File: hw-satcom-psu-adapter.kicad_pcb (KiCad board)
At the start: 2 copper layers, 89.2 x 45 mm, 37 parts, among them J1 Conn_01x04, J2 XT30, J3 XT30, J4 Conn_01x06_MountingPin, J5 s, U1 Brick-DCDC

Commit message: pmbus and normal
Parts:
- U1: footprint alex's:Quarter-Brick -> alex's:Quarter-Brick-PMBus
- moved R7 3.20 mm to (178.7, 82.1)
- moved R10 0.40 mm to (172.4, 95.5)
- moved R9 0.40 mm to (172.4, 98.5)
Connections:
- J5 pad 1: Net-(U1-Pad6) -> Net-(J5-Pad1)
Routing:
- net Net-(J5-Pad1): track 0.00 -> 25.8 mm, vias 0 -> 2
- net PMBus_ALT: track 43.0 -> 63.7 mm, vias 3 -> 2
- net Net-(R8-Pad2): track 0.00 -> 14.3 mm
- net GNDS: track 0.00 -> 12.4 mm
- net Net-(R7-Pad1): track 0.00 -> 11.0 mm
- net I2C_SCL: track 70.2 -> 63.0 mm, vias 1 -> 3
- net I2C_SDA: track 75.1 -> 68.1 mm
- net PMBus_CTL: track 36.1 -> 29.4 mm
- net +3V3: track 63.1 -> 64.6 mm
- net Net-(R10-Pad1): track 3.90 -> 3.29 mm
- net GND2: track 8.12 -> 8.51 mm, vias 2 -> 3

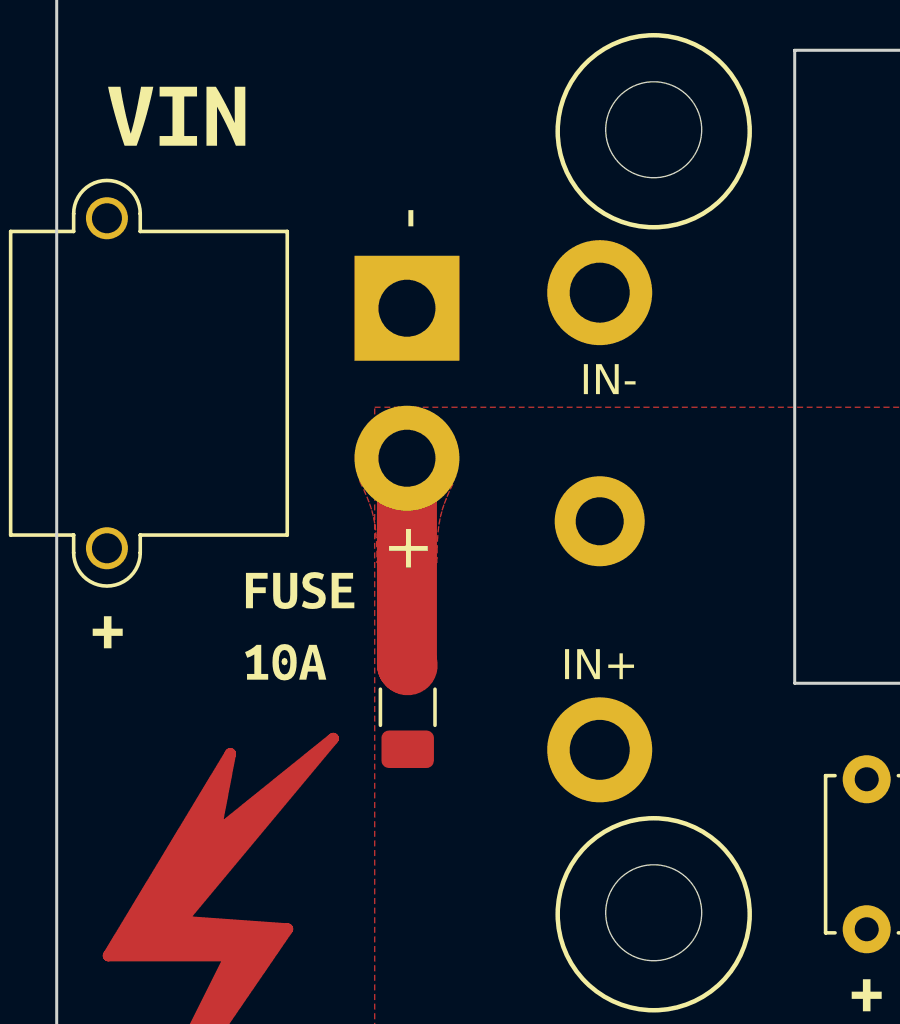
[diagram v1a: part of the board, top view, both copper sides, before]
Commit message: change fuse footprint
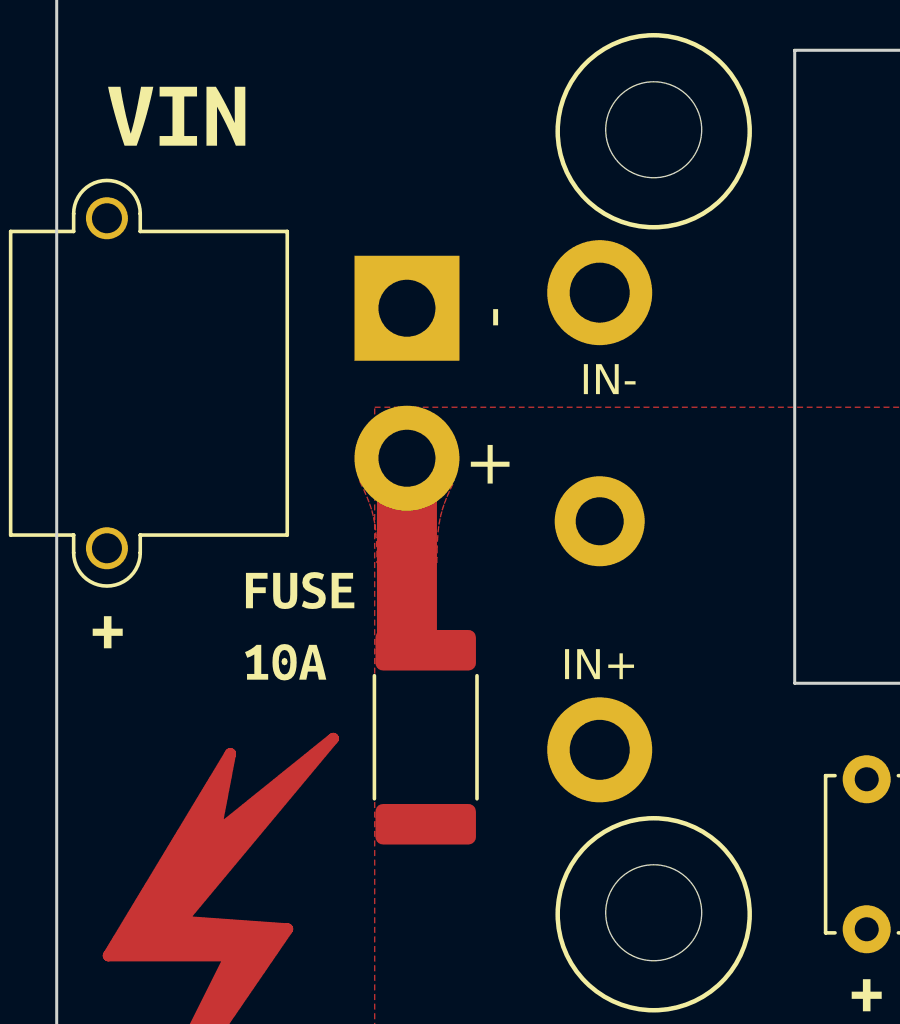
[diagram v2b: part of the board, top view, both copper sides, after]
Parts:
- F1: footprint Fuse:Fuse_1206_3216Metric -> Fuse:Fuse_2512_6332Metric
- moved F1 1.17 mm to (118.7, 104.1)
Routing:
- net Net-(F1-Pad1): track 6.91 -> 5.78 mm
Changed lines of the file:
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@@
       (effects (font (size 1 1) (thickness 0.15)))
     )
-    (fp_text user "-" (at 3 0 90) (layer "F.SilkS")
+    (fp_text user "-" (at -0.3 2.825 90) (layer "F.SilkS")
       (effects (font (size 1.5 1.5) (thickness 0.15)))
     )
-    (fp_text user "+" (at -8 0 90) (layer "F.SilkS")
+    (fp_text user "+" (at -5.2 2.725 90) (layer "F.SilkS")
       (effects (font (size 1.5 1.5) (thickness 0.15)))
     )
@@
     )
   )
-  (footprint "Fuse:Fuse_1206_3216Metric" (layer "F.Cu")
-    (at 118.1 103.1 -90)
-    (descr "Fuse SMD 1206 (3216 Metric), square (rectangular) end terminal, IPC_7351 nominal, (Body size source: http://www.tortai-tech.com/upload/download/2011102023233369053.pdf), generated with kicad-footprint-generator")
+  (footprint "Fuse:Fuse_2512_6332Metric" (layer "F.Cu")
+    (at 118.7 104.1 -90)
+    (descr "Fuse SMD 2512 (6332 Metric), square (rectangular) end terminal, IPC_7351 nominal, (Body size source: http://www.tortai-tech.com/upload/download/2011102023233369053.pdf), generated with kicad-footprint-generator")
     (tags "fuse")
     (property "Sheetfile" "hw-satcom-psu-adapter.kicad_sch")
     (property "Sheetname" "")
     (attr smd)
-    (fp_text reference "F1" (at 0 -1.82 90) (layer "F.SilkS") hide
-      (effects (font (size 1 1) (thickness 0.15)))
-    )
-    (fp_text value "10A" (at 0 1.82 90) (layer "F.Fab")
-      (effects (font (size 1 1) (thickness 0.15)))
-    )
-    (fp_text user "${REFERENCE}" (at 0 0 90) (layer "F.Fab") hide
-      (effects (font (size 0.8 0.8) (thickness 0.12)))
-    )
-    (fp_line (start -0.602064 -0.91) (end 0.602064 -0.91) (layer "F.SilkS") (width 0.12))
-    (fp_line (start -0.602064 0.91) (end 0.602064 0.91) (layer "F.SilkS") (width 0.12))
-    (fp_line (start -2.28 -1.12) (end 2.28 -1.12) (layer "F.CrtYd") (width 0.05))
-    (fp_line (start 2.28 -1.12) (end 2.28 1.12) (layer "F.CrtYd") (width 0.05))
-    (fp_line (start -2.28 1.12) (end -2.28 -1.12) (layer "F.CrtYd") (width 0.05))
-    (fp_line (start 2.28 1.12) (end -2.28 1.12) (layer "F.CrtYd") (width 0.05))
-    (fp_line (start 1.6 -0.8) (end 1.6 0.8) (layer "F.Fab") (width 0.1))
-    (fp_line (start -1.6 -0.8) (end 1.6 -0.8) (layer "F.Fab") (width 0.1))
-    (fp_line (start 1.6 0.8) (end -1.6 0.8) (layer "F.Fab") (width 0.1))
-    (fp_line (start -1.6 0.8) (end -1.6 -0.8) (layer "F.Fab") (width 0.1))
-    (pad "1" smd roundrect (at -1.4 0 270) (size 1.25 1.75) (layers "F.Cu" "F.Paste" "F.Mask") (roundrect_rratio 0.2)
+    (fp_text reference "F1" (at 0 -2.62 -90) (layer "F.SilkS") hide
+      (effects (font (size 1 1) (thickness 0.15)))
+    )
+    (fp_text value "10A" (at 0 2.62 -90) (layer "F.Fab")
+      (effects (font (size 1 1) (thickness 0.15)))
+    )
+    (fp_text user "${REFERENCE}" (at 0 0 -90) (layer "F.Fab")
+      (effects (font (size 1 1) (thickness 0.15)))
+    )
+    (fp_line (start -2.052064 1.71) (end 2.052064 1.71) (layer "F.SilkS") (width 0.12))
+    (fp_line (start -2.052064 -1.71) (end 2.052064 -1.71) (layer "F.SilkS") (width 0.12))
+    (fp_line (start -3.82 -1.92) (end 3.82 -1.92) (layer "F.CrtYd") (width 0.05))
+    (fp_line (start 3.82 -1.92) (end 3.82 1.92) (layer "F.CrtYd") (width 0.05))
+    (fp_line (start -3.82 1.92) (end -3.82 -1.92) (layer "F.CrtYd") (width 0.05))
+    (fp_line (start 3.82 1.92) (end -3.82 1.92) (layer "F.CrtYd") (width 0.05))
+    (fp_line (start -3.15 1.6) (end -3.15 -1.6) (layer "F.Fab") (width 0.1))
+    (fp_line (start 3.15 1.6) (end -3.15 1.6) (layer "F.Fab") (width 0.1))
+    (fp_line (start 3.15 -1.6) (end 3.15 1.6) (layer "F.Fab") (width 0.1))
+    (fp_line (start -3.15 -1.6) (end 3.15 -1.6) (layer "F.Fab") (width 0.1))
+    (pad "1" smd roundrect (at -2.9 0 270) (size 1.35 3.35) (layers "F.Cu" "F.Paste" "F.Mask") (roundrect_rratio 0.185185)
       (net 9 "Net-(F1-Pad1)") (pintype "passive"))
-    (pad "2" smd roundrect (at 1.4 0 270) (size 1.25 1.75) (layers "F.Cu" "F.Paste" "F.Mask") (roundrect_rratio 0.2)
+    (pad "2" smd roundrect (at 2.9 0 270) (size 1.35 3.35) (layers "F.Cu" "F.Paste" "F.Mask") (roundrect_rratio 0.185185)
       (net 1 "/VIN") (pintype "passive"))
-    (model "${KICAD6_3DMODEL_DIR}/Fuse.3dshapes/Fuse_1206_3216Metric.wrl"
+    (model "${KICAD6_3DMODEL_DIR}/Fuse.3dshapes/Fuse_2512_6332Metric.wrl"
       (offset (xyz 0 0 0))
       (scale (xyz 1 1 1))
@@
   (gr_rect (start 177.8 102.5) (end 180.7 87.5) (layer "B.Mask") (width 0.15) (fill solid))
   (gr_circle (center 185.4 82) (end 185.8 82) (layer "B.Mask") (width 0.15) (fill solid))
-  (gr_rect (start 117.1 97.2) (end 119 100.4) (layer "F.Mask") (width 0.15) (fill solid))
+  (gr_rect (start 117.1 97.2) (end 119 99.7) (layer "F.Mask") (width 0.15) (fill solid))
   (gr_rect (start 119 100.4) (end 119 100.4) (layer "F.Mask") (width 0.15) (fill none))
   (gr_rect (start 106.9 103.5) (end 116.1 119.3) (layer "F.Mask") (width 0.15) (fill solid))
   (gr_rect (start 178.1 95.1) (end 180.7 106.5) (layer "F.Mask") (width 0.15) (fill solid))
-  (gr_rect (start 119.8 107.3) (end 121.8 102.9) (layer "F.Mask") (width 0.15) (fill solid))
+  (gr_rect (start 122 110.6) (end 117.6 108.6) (layer "F.Mask") (width 0.15) (fill solid))
   (gr_line (start 131 102.3) (end 136.7 102.3) (layer "Edge.Cuts") (width 0.1))
   (gr_line (start 169.4 113.9) (end 169.4 102.4) (layer "Edge.Cuts") (width 0.1))
@@
   (segment (start 185.6525 88.965) (end 184.07 87.3825) (width 0.25) (layer "F.Cu") (net 8))
   (segment (start 185.7 88.965) (end 185.6525 88.965) (width 0.25) (layer "F.Cu") (net 8))
-  (segment (start 118.075 101.675) (end 118.1 101.7) (width 2) (layer "F.Cu") (net 9))
-  (segment (start 118.075 94.8) (end 118.075 101.675) (width 2) (layer "F.Cu") (net 9))
+  (segment (start 118.075 94.8) (end 118.075 100.575) (width 2) (layer "F.Cu") (net 9))
   (segment (start 189.15 110.775) (end 188.025 110.775) (width 0.2) (layer "F.Cu") (net 10))
   (segment (start 155.58 120.3) (end 154.88 119.6) (width 0.25) (layer "F.Cu") (net 10))

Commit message: ATX
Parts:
- removed C2, C3: 470uF/50V, Capacitor_THT:C_Disc_D5.0mm_W2.5mm_P5.00mm
- removed C4: 1uF/50V, Capacitor_SMD:C_0805_2012Metric
- removed F1: 10A, Fuse:Fuse_2512_6332Metric
- removed H1: MountingHole, MountingHole:MountingHole_2.5mm
- removed R10, R9: NC, Resistor_SMD:R_0603_1608Metric
- removed REF**: Symbol_HighVoltage_Type1_CopperTop_Big, Symbol:Symbol_HighVoltage_Type1_CopperTop_Big
- removed kibuzzard-6276051F: G***, kibuzzard-6276051F
- removed kibuzzard-6276052C: G***, kibuzzard-6276052C
- removed kibuzzard-62760583 (x5): G***, kibuzzard-62760583
- removed kibuzzard-62760647: G***, kibuzzard-62760647
- removed kibuzzard-62760724: G***, kibuzzard-62760724
- removed kibuzzard-62760775: G***, kibuzzard-62760775
- added C10: 470uF/25V, Capacitor_THT:CP_Radial_D6.3mm_P2.50mm, B.Cu at (183.4, 69.8)
- added C12: 470uF/25V, Capacitor_THT:CP_Radial_D6.3mm_P2.50mm, B.Cu at (208.2, 95.4)
- added C13: 470uF/25V, Capacitor_THT:CP_Radial_D6.3mm_P2.50mm, B.Cu at (218.5, 128.1)
- added C14: 100nF/100V, lc:0805_C, F.Cu at (113.7, 120.4)
- added C15: 470uF/25V, Capacitor_THT:CP_Radial_D6.3mm_P2.50mm, B.Cu at (217.5, 69.6)
- added C16: 470uF/25V, Capacitor_THT:CP_Radial_D6.3mm_P2.50mm, B.Cu at (217.4, 79.0)
- added C17: 470uF/25V, Capacitor_THT:CP_Radial_D6.3mm_P2.50mm, B.Cu at (216.6, 95.4)
- added C5: 47nF, lc:0402_C, F.Cu at (104.5, 111.7)
- added C6: 10nF, lc:0402_C, F.Cu at (103.5, 111.7)
- added C7: 470uF/25V, Capacitor_THT:CP_Radial_D6.3mm_P2.50mm, B.Cu at (200.7, 69.8)
- added C8: 470uF/25V, Capacitor_THT:CP_Radial_D6.3mm_P2.50mm, B.Cu at (192.1, 69.8)
- added C9: 470uF/25V, Capacitor_THT:CP_Radial_D6.3mm_P2.50mm, B.Cu at (174.8, 69.8)
- added D10: Green, lc:0805_LED_S1_NUM, F.Cu at (189.1, 128.7)
- added D11: Blue, lc:0805_LED_S1_NUM, F.Cu at (193.1, 128.7)
- added D12: Blue, lc:0805_LED_S1_NUM, F.Cu at (188.9, 119.1)
- added D4: Yellow, lc:0805_LED_S1_NUM, F.Cu at (181.1, 119.1)
- added D5: Yellow, lc:0805_LED_S1_NUM, F.Cu at (185.0, 119.1)
- added D6: 1N5819WS, lc:SOD-323, F.Cu at (162.4, 120.1)
- added D7: 1N5819WS, lc:SOD-323, F.Cu at (160.8, 120.1)
- added D8: Green, lc:0805_LED_S1_NUM, F.Cu at (181.2, 128.7)
- added D9: Green, lc:0805_LED_S1_NUM, F.Cu at (185.2, 128.7)
- added FL1: ACM1513F-551T100, t123yh:ACM1513, F.Cu at (122.7, 116.0)
- added G***: LOGO, LOGO, F.Cu at (160.6, 93.1)
- added H2: SMTSO-M3, MountingHole:MountingHole_4.3mm_M4_Pad, B.Cu at (106.5, 101.8)
- added H3: SMTSO-M3, MountingHole:MountingHole_4.3mm_M4_Pad, B.Cu at (106.4, 61.8)
- added H4: SMTSO-632, MountingHole:MountingHole_5.5mm_Pad, B.Cu at (229.3, 56.5)
- added H5: SMTSO-632, MountingHole:MountingHole_5.5mm_Pad, B.Cu at (91.8, 120.2)
- added H6: SMTSO-632, MountingHole:MountingHole_5.5mm_Pad, B.Cu at (91.5, 56.2)
- added H7: SMTSO-632, MountingHole:MountingHole_5.5mm_Pad, B.Cu at (205.3, 129.7)
- added H8: SMTSO-M3, MountingHole:MountingHole_4.3mm_M4_Pad, F.Cu at (171.6, 129.9)
- added H9: SMTSO-M3, MountingHole:MountingHole_4.3mm_M4_Pad, F.Cu at (122.8, 130.0)
- added J_CPU1: Conn_02x04_Top_Bottom, t123yh:ATX-8P, B.Cu at (201.4, 59.5)
- added J_CPU2: Conn_02x04_Top_Bottom, t123yh:ATX-8P, B.Cu at (180.5, 59.5)
- added Q1: NCE0140K2, Package_TO_SOT_SMD:TO-252-2, F.Cu at (90.1, 106.0)
- added Q2: NCE0140K2, Package_TO_SOT_SMD:TO-252-2, F.Cu at (100.5, 129.5)
- added Q3: NCE0140K2, Package_TO_SOT_SMD:TO-252-2, F.Cu at (97.5, 106.0)
- added Q4: 2N7002, Package_TO_SOT_SMD:SOT-23, F.Cu at (144.7, 120.6)
- added Q5: 2N7002, Package_TO_SOT_SMD:SOT-23, F.Cu at (156.8, 117.1)
- added Q6: 2N7002, Package_TO_SOT_SMD:SOT-23, F.Cu at (197.4, 133.2)
- added R11: 8.2k, lc:0402_R, F.Cu at (105.7, 111.7)
- added R12: 220k, lc:0603_R, F.Cu at (110.7, 107.2)
- added R13: 51k, lc:0402_R, F.Cu at (110.1, 122.2)
- added R14: 120k, lc:0603_R, F.Cu at (134.8, 116.9)
- added R15: 3m, lc:2512_R, F.Cu at (100.6, 117.4)
- added R16: 10k, lc:0402_R, F.Cu at (111.4, 122.2)
- added R17: 220k, lc:0603_R, F.Cu at (121.2, 96.9)
- added R18: 51k, lc:0603_R, F.Cu at (131.1, 118.3)
- added R19: 22k, lc:0402_R, F.Cu at (141.9, 120.7)
- added R20: 5.1k, lc:0402_R, F.Cu at (147.9, 122.1)
- added R21: 5.1k, lc:0402_R, F.Cu at (152.6, 118.5)
- added R22: 8.2k, lc:0402_R, F.Cu at (185.5, 114.7)
- added R23: 22k, lc:0402_R, F.Cu at (163.4, 123.0)
- added R24: 10k, lc:0603_R, F.Cu at (161.7, 117.1)
- added R25: 390, lc:0603_R, F.Cu at (214.4, 64.8)
- added R26: 100, lc:0402_R, F.Cu at (206.1, 79.1)
- added R27: 100, lc:0402_R, F.Cu at (217.0, 90.7)
- added U10: ZXDN10, t123yh:ZXDN10, B.Cu at (206.8, 90.6)
- added U2: TPS2350, Package_SO:TSSOP-14_4.4x5mm_P0.65mm, F.Cu at (106.4, 117.6)
- added U3: EL3H7(B)(TA)-G, Package_SO:SOP-4_4.4x2.6mm_P1.27mm, F.Cu at (108.3, 125.5)
- added U4: EL3H7(B)(TA)-G, Package_SO:SOP-4_4.4x2.6mm_P1.27mm, F.Cu at (136.4, 123.3)
- added U5: AV10-48S05, t123yh:AV10-48Sxx, B.Cu at (141.9, 64.3)
- added U6: EL3H7(B)(TA)-G, Package_SO:SOP-4_4.4x2.6mm_P1.27mm, F.Cu at (136.4, 119.6)
- added U7: TPS3510, Package_SO:SOIC-8_3.9x4.9mm_P1.27mm, F.Cu at (155.0, 121.9)
- added U8: ZXDN10, t123yh:ZXDN10, B.Cu at (214.5, 52.9)
- added U9: ZXDN10, t123yh:ZXDN10, B.Cu at (206.1, 68.9)
- D1: value Yellow -> Green; footprint LED_SMD:LED_0603_1608Metric -> lc:0805_LED_S1_NUM
- D2: value Yellow -> Red; footprint LED_SMD:LED_0603_1608Metric -> lc:0805_LED_S1_NUM
- D3: value Yellow -> 1N4148WS; footprint LED_SMD:LED_0603_1608Metric -> lc:SOD-323
- J1: value Conn_01x04 -> Conn_01x02_Male; footprint Connector_PinSocket_2.54mm:PinSocket_1x04_P2.54mm_Vertical -> Connector_AMASS:AMASS_XT60-M_1x02_P7.20mm_Vertical; moved to F.Cu
- J2: value XT30 -> ATX-24; footprint Connector_AMASS:AMASS_XT30PW-M_1x02_P2.50mm_Horizontal -> t123yh:ATX-24P; moved to B.Cu
- J3: value XT30 -> Conn_02x02_Top_Bottom; footprint Connector_AMASS:AMASS_XT30PW-M_1x02_P2.50mm_Horizontal -> t123yh:ATX-4P; moved to B.Cu
- J4: value Conn_01x06_MountingPin -> Conn_02x02_Top_Bottom; footprint Connector_Molex:Molex_CLIK-Mate_502382-0670_1x06-1MP_P1.25mm_Vertical -> t123yh:ATX-4P; moved to B.Cu
- J5: value s -> Conn_01x02_Male; footprint Connector_Molex:Molex_CLIK-Mate_502382-0370_1x03-1MP_P1.25mm_Vertical -> Connector_AMASS:AMASS_XT60-M_1x02_P7.20mm_Vertical
- R1: value 4.7k -> 200k; footprint Resistor_SMD:R_0603_1608Metric -> lc:0402_R
- R2: value 4.7k -> 22k; footprint Resistor_SMD:R_0603_1608Metric -> lc:0402_R
- R3: value 4.7k -> 56k; footprint Resistor_SMD:R_0603_1608Metric -> lc:0402_R
- R4: value 3.9k -> 56k; footprint Resistor_SMD:R_0603_1608Metric -> lc:0402_R
- R5: value 100k -> 390k; footprint Resistor_SMD:R_0603_1608Metric -> lc:0603_R
- R6: value 47k -> 5.6k; footprint Resistor_SMD:R_0603_1608Metric -> lc:0402_R
- R7, R8: value NC -> 3.3k; footprint Resistor_SMD:R_0603_1608Metric -> lc:0402_R
- kibuzzard-62760563: moved to B.Cu
- moved J2 109.0 mm to (227.0, 93.8)
- moved J5 89.0 mm to (102.7, 74.8), turned to 0 degrees
- moved R6 82.1 mm to (107.2, 112.1), turned to 180 degrees
- moved D3 78.7 mm to (110.3, 115.5), turned to 90 degrees
- moved J1 60.6 mm to (102.7, 88.8), turned to 0 degrees
- moved R7 50.3 mm to (196.3, 129.2)
- moved R8 34.0 mm to (189.4, 114.8), turned to 0 degrees
- moved kibuzzard-62760563 32.8 mm to (97.1, 133.4)
- moved J3 30.1 mm to (212.9, 106.1), turned to 90 degrees
- moved J4 22.1 mm to (212.9, 117.6), turned to 90 degrees
- moved R2 19.5 mm to (198.1, 125.3), turned to 90 degrees
- moved R3 15.5 mm to (196.3, 125.3), turned to 90 degrees
- moved D2 12.2 mm to (108.9, 109.4), turned to 0 degrees
- moved C1 11.3 mm to (132.3, 99.3)
- moved R5 10.1 mm to (109.9, 111.9), turned to 180 degrees
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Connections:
- C1 pad 1: /VIN -> /RTN_FIL
- C1 pad 2: GND1 -> /NEG_FIL
- D1 pad 1: Net-(D1-Pad1) -> GND2
- D1 pad 2: +3V3 -> Net-(D1-Pad2)
- D2 pad 2: /VIN -> Net-(D2-Pad2)
- D3 pad 2: /VOUT -> /RTN
- J1 pad 1: I2C_SCL -> /NEGA
- J1 pad 2: I2C_SDA -> /RTN
- J2 pad 1: GND1 -> +3.3V
- J2 pad 2: Net-(F1-Pad1) -> +3.3V
- J3 pad 2: /VOUT -> +12V
- J4 pad 1: I2C_SCL -> GND2
- J4 pad 2: I2C_SDA -> +12V
- J4 pad 3: PMBus_CTL -> +5VD
- J4 pad 4: PMBus_ALT -> GND2
- J5 pad 1: Net-(J5-Pad1) -> /NEGB
- J5 pad 2: PMBus_ALT -> /RTN
- R1 pad 1: +3V3 -> Net-(D1-Pad2)
- R1 pad 2: I2C_SDA -> +12V
- R2 pad 1: +3V3 -> Net-(D8-Pad2)
- R2 pad 2: I2C_SCL -> +3.3V
- R3 pad 1: +3V3 -> Net-(D9-Pad2)
- R3 pad 2: PMBus_ALT -> +5VA
- R4 pad 1: Net-(D1-Pad1) -> Net-(D10-Pad2)
- R4 pad 2: GNDS -> +5VD
- R5 pad 1: Net-(D2-Pad1) -> /RTN
- R5 pad 2: GND1 -> Net-(R5-Pad2)
- R6 pad 1: Net-(D3-Pad1) -> Net-(R5-Pad2)
- R6 pad 2: GND2 -> Net-(R11-Pad1)
- R7 pad 1: Net-(R7-Pad1) -> Net-(D11-Pad2)
- R7 pad 2: GNDS -> +5VA
- R8 pad 1: GNDS -> Net-(D12-Pad2)
- R8 pad 2: Net-(R8-Pad2) -> +5VA
- U1 pad 2: Net-(R7-Pad1) -> unconnected-(U1-Pad2)
- U1 pad 4: Net-(R8-Pad2) -> unconnected-(U1-Pad4)
- U1 pad 6: Net-(J5-Pad1) -> unconnected-(U1-Pad6)
- U1 pad GATE: /VIN -> Net-(R17-Pad2)
- U1 pad IN+: /VIN -> /RTN_FIL
- U1 pad IN-: GND1 -> /NEG_FIL
- U1 pad OUT+: /VOUT -> +12V
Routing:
- net /+5VSB: track 0.00 -> 300.1 mm, vias 0 -> 6
- net /DCDC_EN: track 0.00 -> 168.1 mm, vias 0 -> 13
- net /PSON: track 0.00 -> 125.7 mm, vias 0 -> 4
- net /NEG: track 0.00 -> 122.1 mm, vias 0 -> 4
- net +5VA: track 0.00 -> 108.6 mm, vias 0 -> 4
- net /PGOOD: track 0.00 -> 104.9 mm, vias 0 -> 3
- net GND2: track 8.51 -> 88.3 mm, vias 3 -> 27
- net +3.3V: track 0.00 -> 75.5 mm, vias 0 -> 2
- net I2C_SDA: track 68.1 -> 0.00 mm, vias 1 -> 0
- net +3V3: track 64.6 -> 0.00 mm, vias 2 -> 0
- net PMBus_ALT: track 63.7 -> 0.00 mm, vias 2 -> 0
- net I2C_SCL: track 63.0 -> 0.00 mm, vias 3 -> 0
- net Net-(R17-Pad2): track 0.00 -> 56.5 mm, vias 0 -> 3
- net /RTN_FIL: track 0.00 -> 53.6 mm
- net Net-(D4-Pad2): track 0.00 -> 47.1 mm, vias 0 -> 2
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- added copper zone on B.Cu, net +12V
- added copper zone on F.Cu, net +12V
- added copper zone on B.Cu, net +3.3V
- added copper zone on B.Cu, net +5VA
- added copper zone on B.Cu, net +5VD
- added copper zone on F.Cu, net /NEG
- added copper zone on F.Cu, net /NEGA
- added copper zone on F.Cu, net /NEGB
- added copper zone on F.Cu, net /NEG_FIL
- added copper zone on F.Cu, net /NEG_SS
- added copper zone on B.Cu, net /RTN
- added copper zone on F.Cu, net /RTN
- added copper zone on F.Cu, net /RTN_FIL
- added copper zone on F.Cu, net GND2
- added copper zone on F.Cu, net Net-(Q2-Pad3)
- removed copper zone on F.Cu, net /VIN
- removed copper zone on F.Cu, net /VOUT
- removed copper zone on B.Cu, net GND1
- removed copper zone on B.Cu, net GNDS
- removed copper zone on F.Cu, net GNDS
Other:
- board size 89.2 x 45 mm -> 149.7 x 85.2 mm
- board text added: "12V"
- board text added: "3V3"
- board text added: "48V"
- board text added: "5V"
- board text added: "5V HD"
- board text added: "5V MB"
- board text added: "5V SB"
- board text added: "5VSB"
- board text added: "A"
- board text added: "B"
- board text added: "GND"
- board text added: "HDD Power"
- board text added: "NC"
- board text added: "NEG (-)"
- board text added: "PG"
- board text added: "PS ON"
- board text added: "PSON"
- board text added: "RTN (+)"
- board text removed: "3V3 GND SDA SCL"
- board text removed: "R"
